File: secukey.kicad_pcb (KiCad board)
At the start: 2 copper layers, 25 x 42 mm, 44 parts, among them SW4 TS-1185-W-4P-H1.8-160, SW5 TS-1185-W-4P-H1.8-160, SW6 TS-1185-W-4P-H1.8-160, U2 RP2350A, U3 NCP1117-3.3_SOT223, U4 W25Q128JVS, U5 ABM8-272-T3_C20625731, U6 SM03B-SRSS-TB, U7 ATECC608A-MAHDA-T

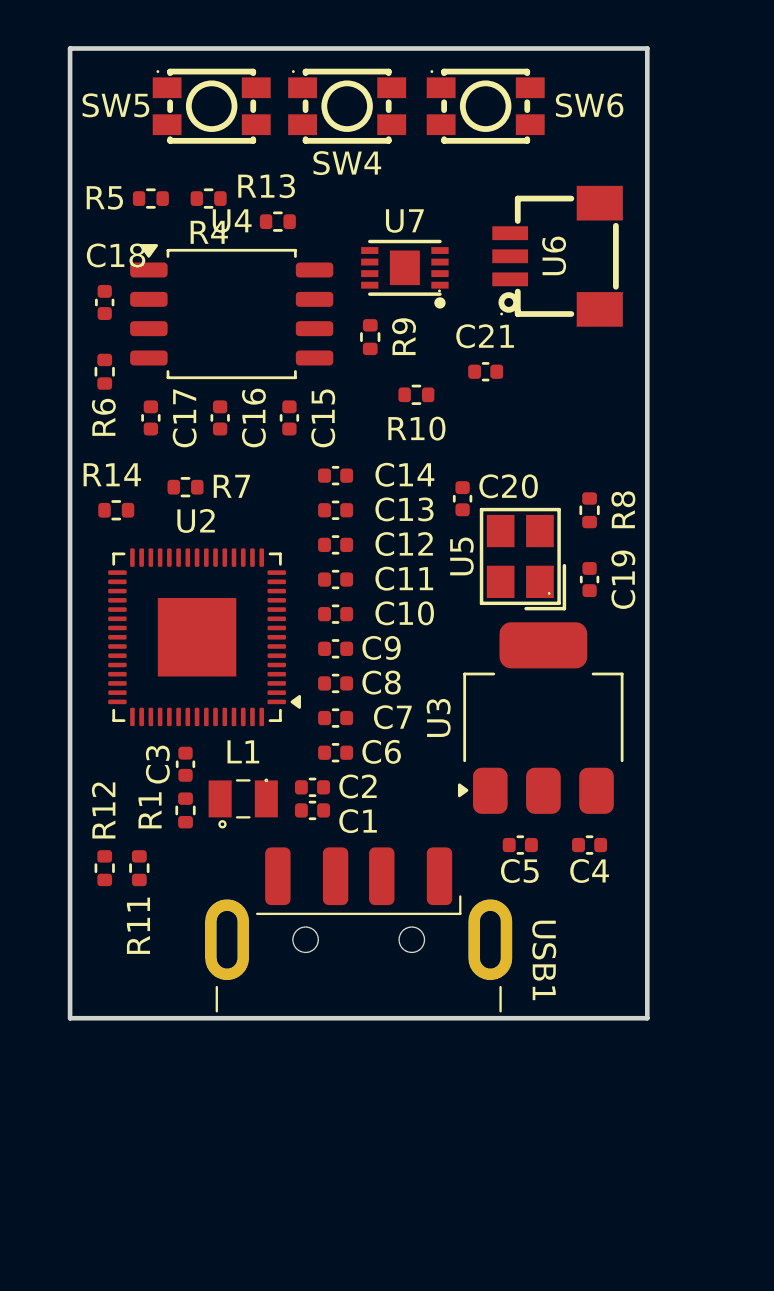
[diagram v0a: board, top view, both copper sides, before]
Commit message: updated capacitor placement
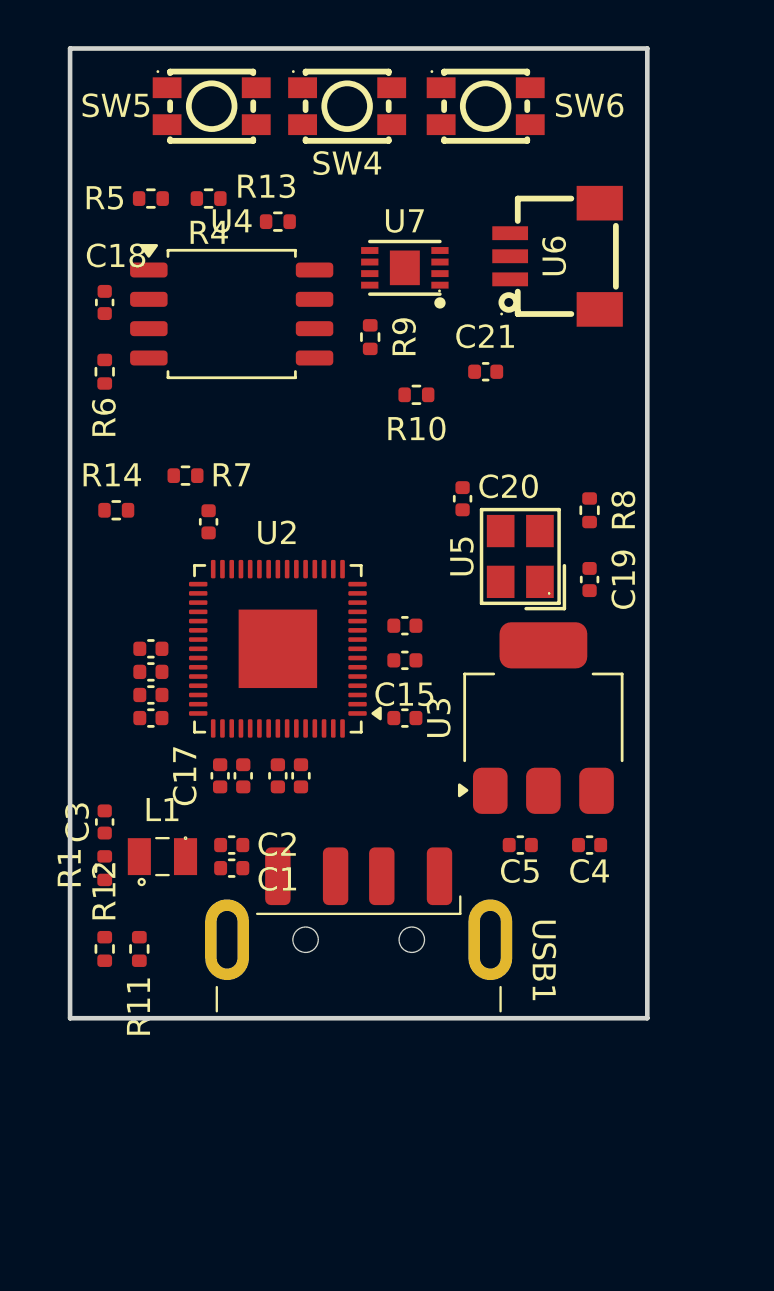
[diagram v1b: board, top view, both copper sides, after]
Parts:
- moved C17 15.8 mm to (151.5, 111.5), turned to -90 degrees
- moved C14 13.1 mm to (155.0, 111.5), turned to -90 degrees
- moved C13 12.0 mm to (148.5, 109.0)
- moved C15 11.6 mm to (159.5, 106.5), turned to 0 degrees
- moved C16 11.4 mm to (148.5, 107.0), turned to 180 degrees
- moved C12 9.18 mm to (148.5, 106.0)
- moved C6 8.38 mm to (148.5, 108.0)
- moved C11 6.04 mm to (151.0, 100.5), turned to -90 degrees
- moved C7 4.72 mm to (152.5, 111.5), turned to -90 degrees
- moved C8 4.72 mm to (154.0, 111.5), turned to -90 degrees
- moved C1 4.30 mm to (152.0, 115.5)
- moved C2 4.30 mm to (152.0, 114.5)
- moved C3 4.30 mm to (146.5, 113.5)
- moved L1 4.30 mm to (149.0, 115.0)
- moved R1 4.30 mm to (146.5, 115.5)
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
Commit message: rearrange the placement for power route
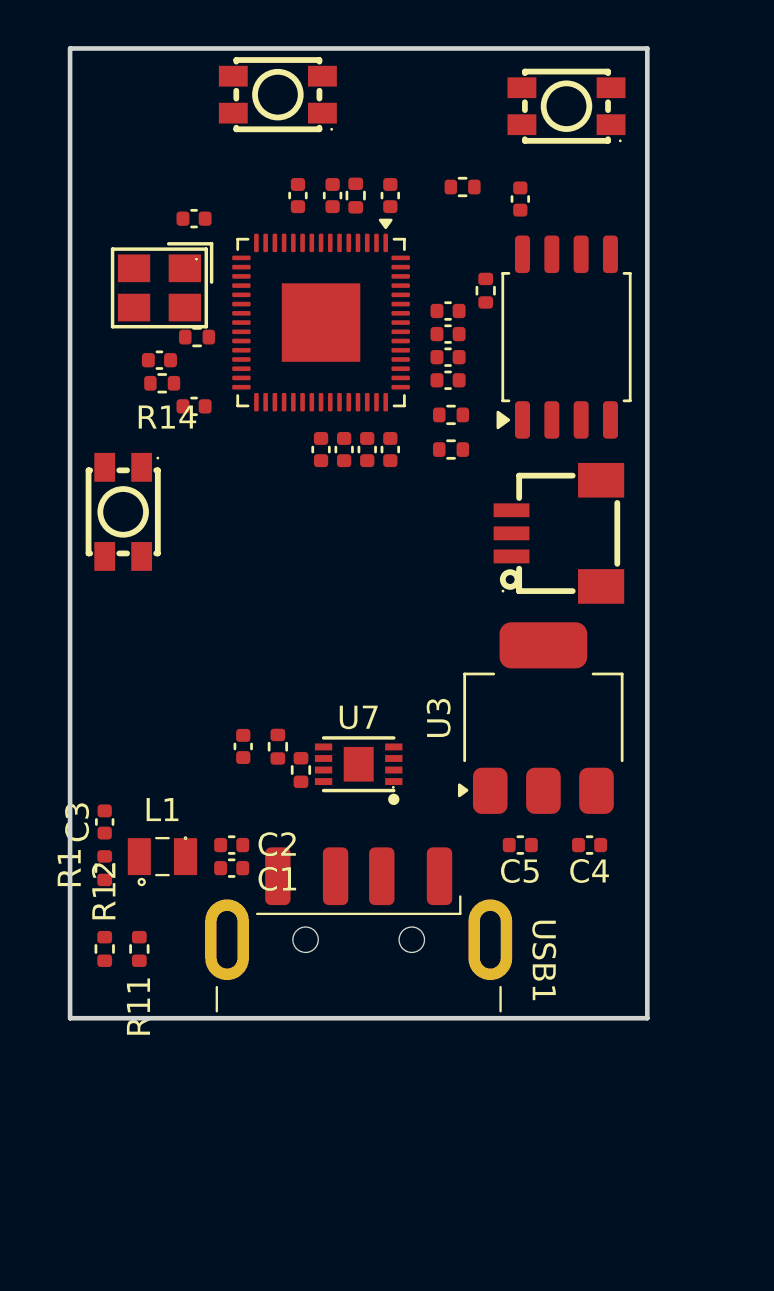
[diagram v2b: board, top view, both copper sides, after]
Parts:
- moved C19 23.2 mm to (150.4, 87.4), turned to 180 degrees
- moved C9 22.6 mm to (158.9, 86.4), turned to -90 degrees
- moved U7 21.6 mm to (157.5, 111.0)
- moved C14 21.1 mm to (161.4, 91.4), turned to 0 degrees
- moved C8 20.5 mm to (161.4, 92.4), turned to 0 degrees
- moved C15 20.4 mm to (156.4, 86.4), turned to 90 degrees
- moved C7 20.2 mm to (161.4, 93.4), turned to 0 degrees
- moved SW4 20.1 mm to (147.3, 100.1), turned to -90 degrees
- moved C17 19.8 mm to (161.4, 94.4), turned to 0 degrees
- moved U5 19.5 mm to (148.9, 90.4), turned to 180 degrees
- moved C21 19.3 mm to (152.5, 110.2), turned to -90 degrees
- moved C10 19.2 mm to (154.9, 86.4), turned to -90 degrees
- moved R8 18.6 mm to (150.5, 92.5), turned to 0 degrees
- moved C18 18.5 mm to (164.5, 86.5)
- moved R9 18.2 mm to (154.0, 110.2)
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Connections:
- SW4 pad 1: unconnected-(SW4-Pad1) -> RP2350B_VREG-PGND
- SW4 pad 2: RP2350B_VREG-PGND -> unconnected-(SW4-Pad2)
- SW4 pad 3: Net-(R14-Pad1) -> unconnected-(SW4-Pad3)
- SW4 pad 4: unconnected-(SW4-Pad4) -> Net-(R14-Pad1)

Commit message: adding ref
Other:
- rule pad_to_mask_clearance: 0.05 -> 0.1
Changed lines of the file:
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@@
 	(layers
 		(0 "F.Cu" signal)
-		(2 "B.Cu" signal)
+		(2 "B.Cu" power)
 		(9 "F.Adhes" user "F.Adhesive")
 		(11 "B.Adhes" user "B.Adhesive")
@@
 		(35 "F.Fab" user)
 		(33 "B.Fab" user)
-		(39 "User.1" user)
-		(41 "User.2" user)
-		(43 "User.3" user)
-		(45 "User.4" user)
 	)
 	(setup
@@
 				(type "Bottom Silk Screen")
 			)
-			(copper_finish "None")
+			(copper_finish "HAL lead-free")
 			(dielectric_constraints no)
 		)
-		(pad_to_mask_clearance 0.05)
+		(pad_to_mask_clearance 0.1)
+		(solder_mask_min_width 0.1)
 		(allow_soldermask_bridges_in_footprints no)
 		(tenting

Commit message: adding made placement
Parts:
- removed C10, C11, C12, C13, C14, C15, C16, C18, C7, C8, C9: 100n, Capacitor_SMD:C_0402_1005Metric
- removed C17, C3: 4.7u, Capacitor_SMD:C_0402_1005Metric
- removed C19, C20: 15p, Capacitor_SMD:C_0402_1005Metric
- removed C21: 100nF, Capacitor_SMD:C_0402_1005Metric
- removed R11, R12: 27, Resistor_SMD:R_0402_1005Metric
- added C22: CC0402KRX7R5BB104, EasyEDA:C0402, F.Cu at (163.0, 109.4)
- added C23: CC0402KRX7R5BB104, EasyEDA:C0402, F.Cu at (168.8, 112.9)
- added C24: CC0402KRX7R5BB104, EasyEDA:C0402, F.Cu at (166.0, 120.0)
- added C25: CC0402KRX7R5BB104, EasyEDA:C0402, F.Cu at (157.8, 112.3)
- added C26: CC0402KRX7R5BB104, EasyEDA:C0402, F.Cu at (168.8, 111.7)
- added C27: CC0402KRX7R5BB104, EasyEDA:C0402, F.Cu at (168.5, 115.6)
- added C28: CC0402KRX7R5BB104, EasyEDA:C0402, F.Cu at (164.8, 109.8)
- added C29: CC0402KRX7R5BB104, EasyEDA:C0402, F.Cu at (161.4, 120.2)
- added C30: CC0402KRX7R5BB104, EasyEDA:C0402, F.Cu at (157.8, 116.2)
- added C31: CC0402KRX7R5BB104, EasyEDA:C0402, F.Cu at (168.5, 114.4)
- added C32: CC0402KRX7R5BB104, EasyEDA:C0402, F.Cu at (163.2, 120.4)
- added C33: CC0402KRX7R5BB104, EasyEDA:C0402, F.Cu at (157.9, 114.2)
- added C34: CC0402KRX7R5BB104, EasyEDA:C0402, F.Cu at (146.8, 99.0)
- added C35: CC0402KRX7R5BB104, EasyEDA:C0402, F.Cu at (149.8, 113.1)
- added C36: CC0402KRX7R5BB104, EasyEDA:C0402, F.Cu at (150.0, 86.0)
- added C37: CC0402KRX7R5BB104, EasyEDA:C0402, F.Cu at (149.8, 91.6)
- added R2: 0805W8J0330T5E, EasyEDA:R0805, F.Cu at (170.3, 108.4)
- added R3: 0805W8F4701T5E, EasyEDA:R0805, F.Cu at (152.1, 118.7)
- C1, C2: value 4.7u -> FCC0805N150J500BT; footprint Capacitor_SMD:C_0402_1005Metric -> EasyEDA:C0805
- C4, C5: value 10u -> CL21A475KBQNNNE; footprint Capacitor_SMD:C_0402_1005Metric -> EasyEDA:C0805
- C6: value 100n -> CL21A475KBQNNNE; footprint Capacitor_SMD:C_0402_1005Metric -> EasyEDA:C0805
- R1: value 33Ω -> RC0805JR-0710KL; footprint Resistor_SMD:R_0402_1005Metric -> EasyEDA:R0805
- R10: value 4,7kΩ -> RC0805JR-071KL; footprint Resistor_SMD:R_0402_1005Metric -> EasyEDA:R0805
- R13: value 10kΩ -> RC0805JR-071KL; footprint Resistor_SMD:R_0402_1005Metric -> EasyEDA:R0805
- R14: value 1k -> RC0805JR-071KL; footprint Resistor_SMD:R_0402_1005Metric -> EasyEDA:R0805
- R6: value 0 -> FRC0805F27R0TS; footprint Resistor_SMD:R_0402_1005Metric -> EasyEDA:R0805
- R7: value 1k -> 0805W8F0000T5E; footprint Resistor_SMD:R_0402_1005Metric -> EasyEDA:R0805
- R8: value 1k -> FRC0805F27R0TS; footprint Resistor_SMD:R_0402_1005Metric -> EasyEDA:R0805
- R9: value 4,7kΩ -> 0805W8F4701T5E; footprint Resistor_SMD:R_0402_1005Metric -> EasyEDA:R0805
- moved USB1 49.0 mm to (159.6, 76.5), turned to 90 degrees
- moved SW5 44.4 mm to (147.8, 126.0)
- moved R13 39.9 mm to (160.6, 126.1), turned to -90 degrees
- moved R14 32.9 mm to (164.8, 123.3)
- moved U5 32.8 mm to (155.7, 122.5), turned to -90 degrees
- moved SW4 29.6 mm to (170.6, 118.4), turned to 0 degrees
- moved U2 24.3 mm to (163.2, 115.0), turned to 0 degrees
- moved U6 23.3 mm to (169.8, 124.0)
- moved R10 22.8 mm to (167.4, 92.1)
- moved U4 22.4 mm to (148.3, 105.5), turned to -90 degrees
- moved R8 19.3 mm to (168.5, 99.5), turned to 90 degrees
- moved L1 18.3 mm to (162.6, 102.7), turned to 0 degrees
- moved U3 18.1 mm to (156.9, 93.1), turned to 180 degrees
- moved R7 17.8 mm to (149.3, 98.5), turned to -90 degrees
- moved R4 15.0 mm to (151.0, 99.5)
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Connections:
- C1 pad 1: RP2350B_VREG-VIN -> Net-(C1-Pad1)
- C2 pad 1: RP2350B_VREG-FB -> RP2350B_VREG-PGND
- C2 pad 2: RP2350B_VREG-PGND -> RP2350B_XIN
- C4 pad 1: VBUS -> RP2350B_VREG-AVDD
- C5 pad 1: RP2350B_VREG-VIN -> RP2350B_VREG-FB
- R1 pad 1: RP2350B_VREG-VIN -> RP2350B_GPIO2
- R1 pad 2: RP2350B_VREG-AVDD -> RP2350B_VREG-VIN
- R10 pad 1: RP2350B_GPIO5 -> Net-(R10-Pad1)
- R10 pad 2: RP2350B_VREG-VIN -> RP2350B_QSPI_SS
- R13 pad 1: RP2350B_GPIO2 -> Net-(C1-Pad1)
- R13 pad 2: RP2350B_VREG-VIN -> RP2350B_XOUT
- R14 pad 1: Net-(R14-Pad1) -> Net-(U2-RUN)
- R14 pad 2: Net-(U2-RUN) -> Net-(R14-Pad2)
- R6 pad 1: RP2350B_QSPI_SS -> Net-(U2-USB_DP)
- R6 pad 2: Net-(U4-~{CS}) -> /USB_D-
- R7 pad 1: Net-(R7-Pad1) -> RP2350B_QSPI_SS
- R7 pad 2: RP2350B_QSPI_SS -> Net-(U4-~{CS})
- R8 pad 1: Net-(C20-Pad2) -> Net-(U2-USB_DM)
- R8 pad 2: RP2350B_XOUT -> /USB_D+
- SW4 pad 4: Net-(R14-Pad1) -> Net-(R14-Pad2)
- SW6 pad 3: Net-(R7-Pad1) -> Net-(R10-Pad1)
- U2 pad 7: unconnected-(U2-GPIO4-Pad7) -> RP2350B_GPIO4
- U2 pad 8: unconnected-(U2-GPIO5-Pad8) -> RP2350B_GPIO5
- U4 pad 2: unconnected-(U4-DO/IO_{1}-Pad2) -> RP2350B_QSPI_SD1
- U4 pad 3: unconnected-(U4-~{WP}/IO_{2}-Pad3) -> RP2350B_QSPI_SD2
- U4 pad 5: unconnected-(U4-DI/IO_{0}-Pad5) -> RP2350B_QSPI_SD0
- U4 pad 7: unconnected-(U4-~{HOLD}/~{RESET}/IO_{3}-Pad7) -> RP2350B_QSPI_SD3
- U5 pad 3: Net-(C20-Pad2) -> Net-(C1-Pad1)
- U7 pad 1: unconnected-(U7-NC-Pad1) -> RP2350B_VREG-PGND
- U7 pad 2: unconnected-(U7-NC-Pad2) -> RP2350B_VREG-PGND
- U7 pad 3: unconnected-(U7-NC-Pad3) -> RP2350B_VREG-PGND
- U7 pad 7: unconnected-(U7-NC-Pad7) -> RP2350B_VREG-PGND
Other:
- board size 25 x 42 mm -> 29 x 49 mm
